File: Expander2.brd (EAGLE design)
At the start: 52.3 x 44.6 mm, 4 parts, among them K2 G5L, K4 G5L

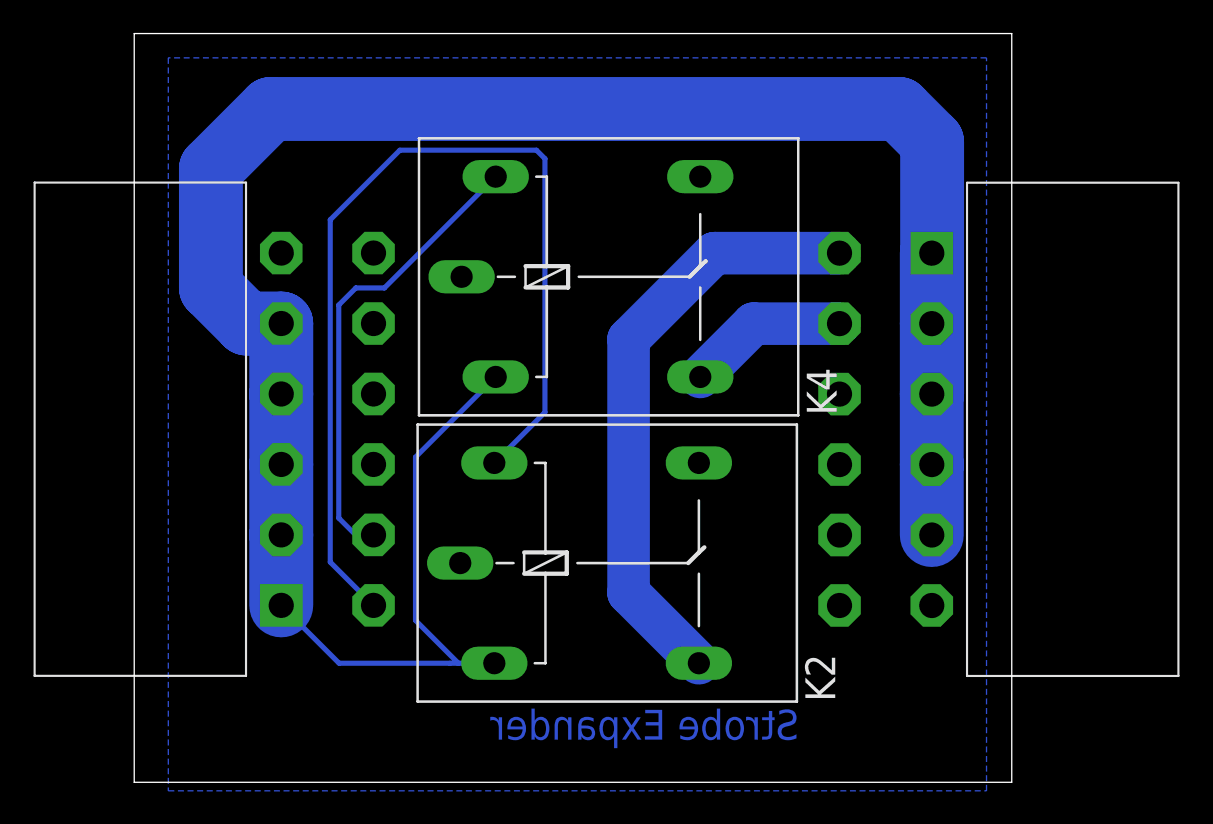
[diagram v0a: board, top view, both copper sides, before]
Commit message: Protective diodes added in expander
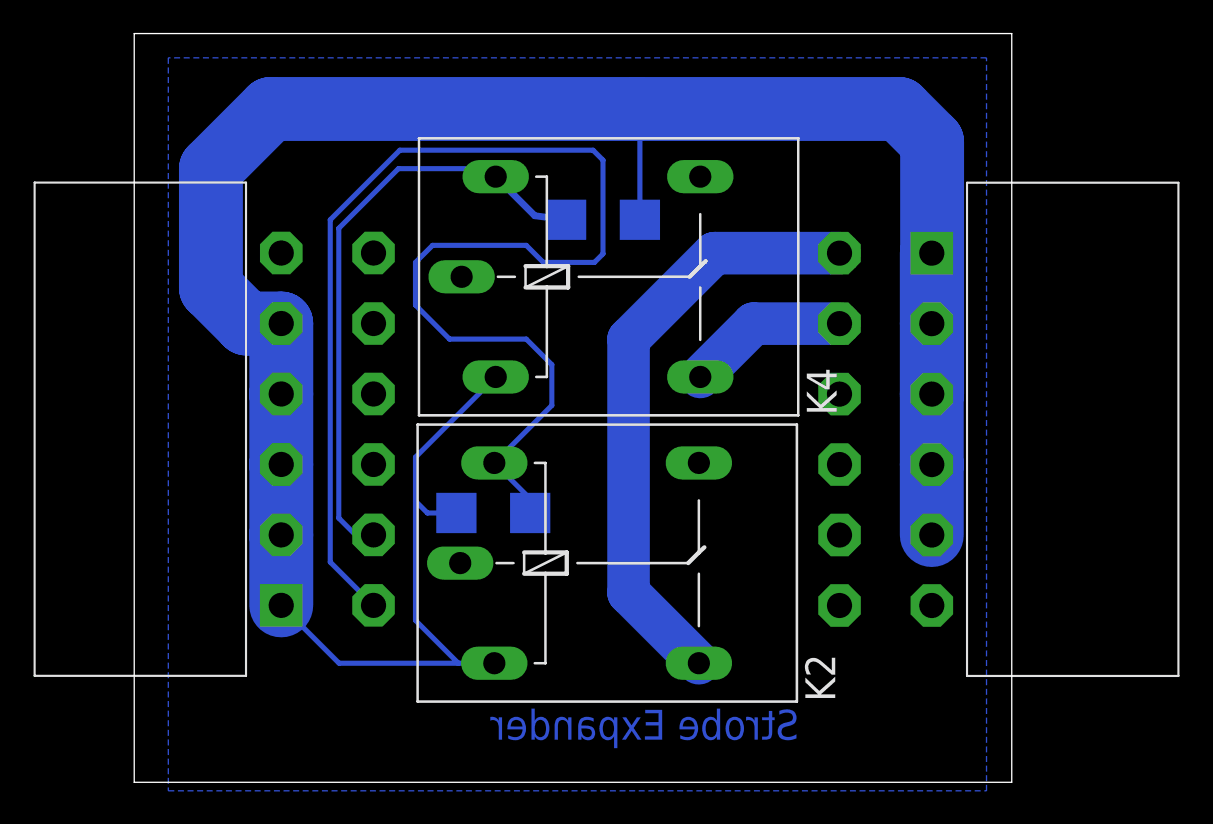
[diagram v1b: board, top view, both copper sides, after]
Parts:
- added D1, D2: (no value), SparkFun-DiscreteSemi:SMB-DIODE
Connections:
- net 12V: now also D1.C, D2.C
- net L3: now also D2.A
- net L4: now also D1.A
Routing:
- net L4: track 58.2 -> 83.5 mm
- net 12V: track 140.3 -> 149.7 mm
- net L3: track 27.7 -> 36.0 mm
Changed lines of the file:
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@@
 </element>
 <element name="OUT" library="con-amphenol" package="MF42-10" value="MF42-10" x="47.538" y="14.23" rot="R90"/>
+<element name="D1" library="SparkFun-DiscreteSemi" package="SMB-DIODE" value="" x="21.402040625" y="15.544803125" rot="MR180"/>
+<element name="D2" library="SparkFun-DiscreteSemi" package="SMB-DIODE" value="" x="27.94" y="33.02" rot="MR0"/>
 </elements>
 <signals>
@@
 <wire x1="47.55641875" y1="22.64841875" x2="47.55641875" y2="37.665659375" width="3.81" layer="16"/>
 <wire x1="47.55641875" y1="37.665659375" x2="45.598078125" y2="39.624" width="3.81" layer="16"/>
-<wire x1="45.598078125" y1="39.624" x2="8.128" y2="39.624" width="3.81" layer="16"/>
+<wire x1="45.598078125" y1="39.624" x2="29.972" y2="39.624" width="3.81" layer="16"/>
+<wire x1="29.972" y1="39.624" x2="8.128" y2="39.624" width="3.81" layer="16"/>
 <wire x1="8.128" y1="39.624" x2="4.572" y2="36.068" width="3.81" layer="16"/>
 <wire x1="4.572" y1="36.068" x2="4.572" y2="28.956" width="3.81" layer="16"/>
@@
 <wire x1="8.763" y1="14.237" x2="8.763" y2="10.037" width="3.81" layer="16"/>
 <wire x1="8.763" y1="10.037" x2="12.211" y2="6.589" width="0.3048" layer="16"/>
-<wire x1="12.211" y1="6.589" x2="18.811" y2="6.589" width="0.3048" layer="16"/>
-<wire x1="18.811" y1="6.589" x2="19.319" y2="6.589" width="0.3048" layer="16"/>
-<wire x1="19.812" y1="6.589" x2="21.463" y2="6.589" width="0.3048" layer="16"/>
+<wire x1="12.211" y1="6.589" x2="19.319" y2="6.589" width="0.3048" layer="16"/>
+<wire x1="19.319" y1="6.589" x2="21.463" y2="6.589" width="0.3048" layer="16"/>
 <wire x1="21.54621875" y1="23.65221875" x2="16.764" y2="18.87" width="0.3048" layer="16"/>
-<wire x1="16.764" y1="18.87" x2="16.764" y2="9.144" width="0.3048" layer="16"/>
+<wire x1="16.764" y1="18.87" x2="16.764" y2="16.256" width="0.3048" layer="16"/>
+<wire x1="16.764" y1="16.256" x2="16.764" y2="9.144" width="0.3048" layer="16"/>
 <wire x1="16.764" y1="9.144" x2="19.319" y2="6.589" width="0.3048" layer="16"/>
-<wire x1="19.319" y1="6.589" x2="19.812" y2="6.589" width="0.3048" layer="16"/>
+<contactref element="D1" pad="C"/>
+<contactref element="D2" pad="C"/>
+<wire x1="30.14" y1="33.02" x2="30.14" y2="39.456" width="0.3048" layer="16"/>
+<wire x1="30.14" y1="39.456" x2="29.972" y2="39.624" width="0.3048" layer="16"/>
+<wire x1="19.202040625" y1="15.544803125" x2="17.475196875" y2="15.544803125" width="0.3048" layer="16"/>
+<wire x1="17.475196875" y1="15.544803125" x2="16.764" y2="16.256" width="0.3048" layer="16"/>
 </signal>
 <signal name="GND">
@@
 <contactref element="IN" pad="8"/>
 <contactref element="K4" pad="2"/>
-<wire x1="21.54621875" y1="35.59021875" x2="14.912" y2="28.956" width="0.3048" layer="16"/>
-<wire x1="14.912" y1="28.956" x2="13.208" y2="28.956" width="0.3048" layer="16"/>
-<wire x1="13.208" y1="28.956" x2="12.192" y2="27.94" width="0.3048" layer="16"/>
-<wire x1="12.192" y1="27.94" x2="12.192" y2="15.24" width="0.3048" layer="16"/>
+<wire x1="12.192" y1="32.512" x2="12.192" y2="15.24" width="0.3048" layer="16"/>
 <wire x1="12.192" y1="15.24" x2="13.195" y2="14.237" width="0.3048" layer="16"/>
 <wire x1="13.195" y1="14.237" x2="14.263" y2="14.237" width="0.3048" layer="16"/>
+<contactref element="D2" pad="A"/>
+<wire x1="25.74" y1="33.02" x2="23.876" y2="33.2604375" width="0.4064" layer="16"/>
+<wire x1="23.876" y1="33.2604375" x2="21.54621875" y2="35.59021875" width="0.4064" layer="16"/>
+<wire x1="12.192" y1="32.512" x2="15.748" y2="36.068" width="0.3048" layer="16"/>
+<wire x1="15.748" y1="36.068" x2="21.0684375" y2="36.068" width="0.3048" layer="16"/>
+<wire x1="21.0684375" y1="36.068" x2="21.54621875" y2="35.59021875" width="0.3048" layer="16"/>
 </signal>
 <signal name="L4">
 <contactref element="IN" pad="7"/>
 <contactref element="K2" pad="2"/>
-<wire x1="21.463" y1="18.527" x2="24.48051875" y2="21.54451875" width="0.3048" layer="16"/>
-<wire x1="24.48051875" y1="21.54451875" x2="24.48051875" y2="36.662359375" width="0.3048" layer="16"/>
-<wire x1="24.48051875" y1="36.662359375" x2="23.975059375" y2="37.16781875" width="0.3048" layer="16"/>
-<wire x1="23.975059375" y1="37.16781875" x2="15.83181875" y2="37.16781875" width="0.3048" layer="16"/>
 <wire x1="15.83181875" y1="37.16781875" x2="11.684" y2="33.02" width="0.3048" layer="16"/>
 <wire x1="11.684" y1="33.02" x2="11.684" y2="12.616" width="0.3048" layer="16"/>
 <wire x1="11.684" y1="12.616" x2="14.263" y2="10.037" width="0.3048" layer="16"/>
+<contactref element="D1" pad="A"/>
+<wire x1="21.463" y1="18.527" x2="21.575" y2="18.527" width="0.3048" layer="16"/>
+<wire x1="24.892" y1="24.384" x2="23.368" y2="25.908" width="0.3048" layer="16"/>
+<wire x1="23.368" y1="25.908" x2="18.796" y2="25.908" width="0.3048" layer="16"/>
+<wire x1="18.796" y1="25.908" x2="16.764" y2="27.94" width="0.3048" layer="16"/>
+<wire x1="16.764" y1="27.94" x2="16.764" y2="30.48" width="0.3048" layer="16"/>
+<wire x1="16.764" y1="30.48" x2="17.78" y2="31.496" width="0.3048" layer="16"/>
+<wire x1="17.78" y1="31.496" x2="23.368" y2="31.496" width="0.3048" layer="16"/>
+<wire x1="23.368" y1="31.496" x2="24.384" y2="30.48" width="0.3048" layer="16"/>
+<wire x1="24.384" y1="30.48" x2="27.432" y2="30.48" width="0.3048" layer="16"/>
+<wire x1="27.432" y1="30.48" x2="27.94" y2="30.988" width="0.3048" layer="16"/>
+<wire x1="27.94" y1="30.988" x2="27.94" y2="36.576" width="0.3048" layer="16"/>
+<wire x1="24.892" y1="21.956" x2="21.463" y2="18.527" width="0.3048" layer="16"/>
+<wire x1="24.892" y1="24.384" x2="24.892" y2="21.956" width="0.3048" layer="16"/>
+<wire x1="15.83181875" y1="37.16781875" x2="27.34818125" y2="37.16781875" width="0.3048" layer="16"/>
+<wire x1="27.34818125" y1="37.16781875" x2="27.94" y2="36.576" width="0.3048" layer="16"/>
+<wire x1="23.602040625" y1="15.544803125" x2="23.536" y2="16.454" width="0.3048" layer="16"/>
+<wire x1="23.536" y1="16.454" x2="21.463" y2="18.527" width="0.3048" layer="16"/>
 </signal>
 <signal name="O3">
